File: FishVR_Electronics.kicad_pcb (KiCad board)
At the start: 2 copper layers, 147.3 x 96.5 mm, 17 parts, among them P1 GND, P2 Vcc, P3 Vsig, U1 CD74HC4067, U2 CD74HC4067, U3 CD74HC4067, U4 CD74HC4067, U5 CD74HC4067, U6 CD74HC4067, U7 CD74HC4067

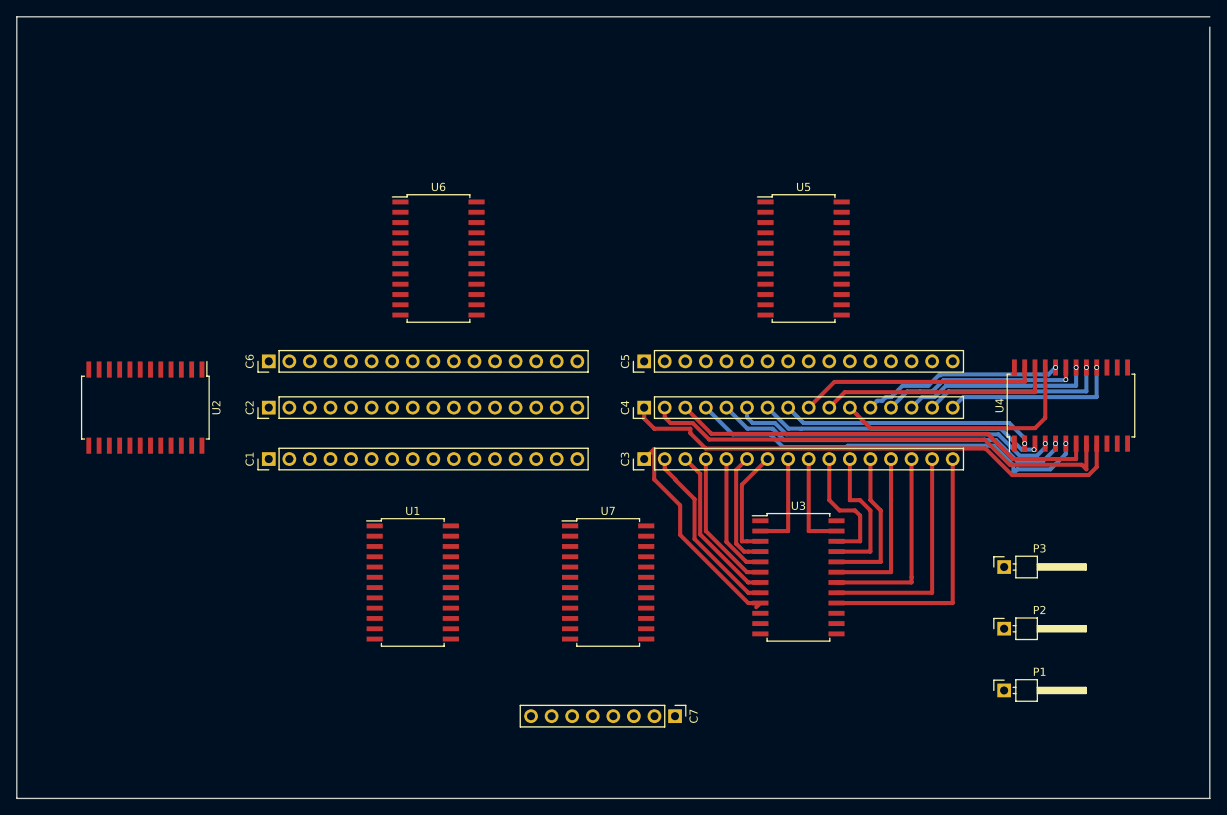
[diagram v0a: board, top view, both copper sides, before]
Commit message: Add files via upload
completed board with traces
still need to add power and ground planes
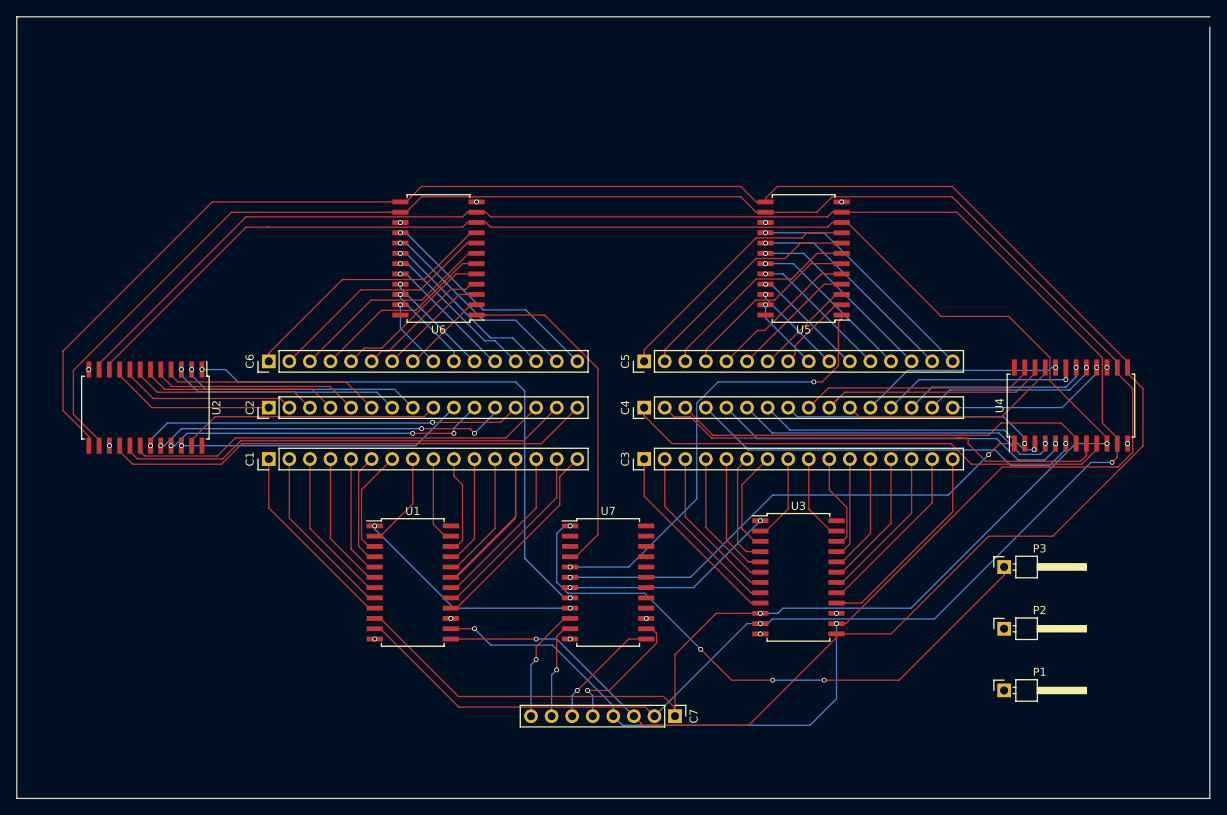
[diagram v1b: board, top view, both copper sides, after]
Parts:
- turned U5 to 180 degrees
- turned U6 to 180 degrees
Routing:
- net Net-(C7-Pad4): track 0.00 -> 279.6 mm, vias 0 -> 2
- net Net-(C7-Pad3): track 0.00 -> 279.3 mm, vias 0 -> 1
- net Net-(C7-Pad2): track 0.00 -> 262.7 mm, vias 0 -> 2
- net Net-(C7-Pad1): track 0.00 -> 260.6 mm, vias 0 -> 2
- net Vsig: track 0.00 -> 74.7 mm, vias 0 -> 4
- net Net-(U2-Pad1): track 0.00 -> 69.2 mm, vias 0 -> 2
- net Net-(U4-Pad1): track 0.00 -> 61.7 mm, vias 0 -> 2
- net Net-(C2-Pad16): track 0.00 -> 60.8 mm
- net Net-(U5-Pad1): track 0.00 -> 56.8 mm, vias 0 -> 2
- net Net-(C2-Pad15): track 0.00 -> 56.4 mm
- net Net-(C2-Pad14): track 0.00 -> 52.3 mm
- net Net-(C2-Pad13): track 0.00 -> 47.4 mm, vias 0 -> 2
- net Net-(C2-Pad12): track 0.00 -> 44.1 mm, vias 0 -> 3
- net Net-(U6-Pad1): track 0.00 -> 42.8 mm
- net Net-(C2-Pad11): track 0.00 -> 39.8 mm, vias 0 -> 3
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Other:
- net class 1 added: clearance 0.2, trace_width 0.1524, via_dia 0.6, via_drill 0.4
- rule trace_min: 0.2 -> 0.1524
- rule via_min_drill: 0.3 -> 0.3048
- board text added: "."

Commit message: finished traces and completed DRC. Ground/ power planes were not effective, so used traces instead.
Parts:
- renumbered P1 to GND, P3 to Signal, P2 to V+
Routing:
- net GND: track 0.00 -> 297.1 mm, vias 14 -> 17
- net +5V: track 0.00 -> 250.0 mm, vias 0 -> 13
- net Vsig: track 74.7 -> 278.1 mm
- net Net-(C7-Pad2): track 262.7 -> 398.8 mm
- net Net-(U2-Pad1): track 69.2 -> 88.3 mm
- net Net-(C4-Pad5): track 44.6 -> 55.6 mm
- net Net-(C4-Pad4): track 49.0 -> 59.4 mm, vias 1 -> 2
- net Net-(C7-Pad1): track 260.6 -> 269.3 mm
- net Net-(C7-Pad4): track 279.6 -> 283.3 mm
- net Net-(C6-Pad8): track 10.8 -> 13.5 mm
- net Net-(C2-Pad12): track 44.1 -> 46.4 mm
- net Net-(C4-Pad8): track 31.5 -> 33.3 mm
- net Net-(U5-Pad1): track 56.8 -> 58.5 mm
- net Net-(C2-Pad13): track 47.4 -> 49.1 mm
- net Net-(C7-Pad3): track 279.3 -> 280.9 mm
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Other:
- board size 147.3 x 96.5 mm -> 136.5 x 71.1 mm
- board text added: "FishVR 2018 96 Electrode Channels"
- board text added: "Microcontroller"
- board text added: "electrode"
- board text added: "s0"
- board text added: "s1"
- board text added: "s2"
- board text added: "s3"
- board text added: "section"
